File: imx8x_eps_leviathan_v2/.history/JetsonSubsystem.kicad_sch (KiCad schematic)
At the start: 32 parts, among them CN1 DF11-16DP-2DSA(08), U13 TPS1HB08BQPWPRQ1, U14 LT8612EUDE#PBF, U15 INA260AIPWR

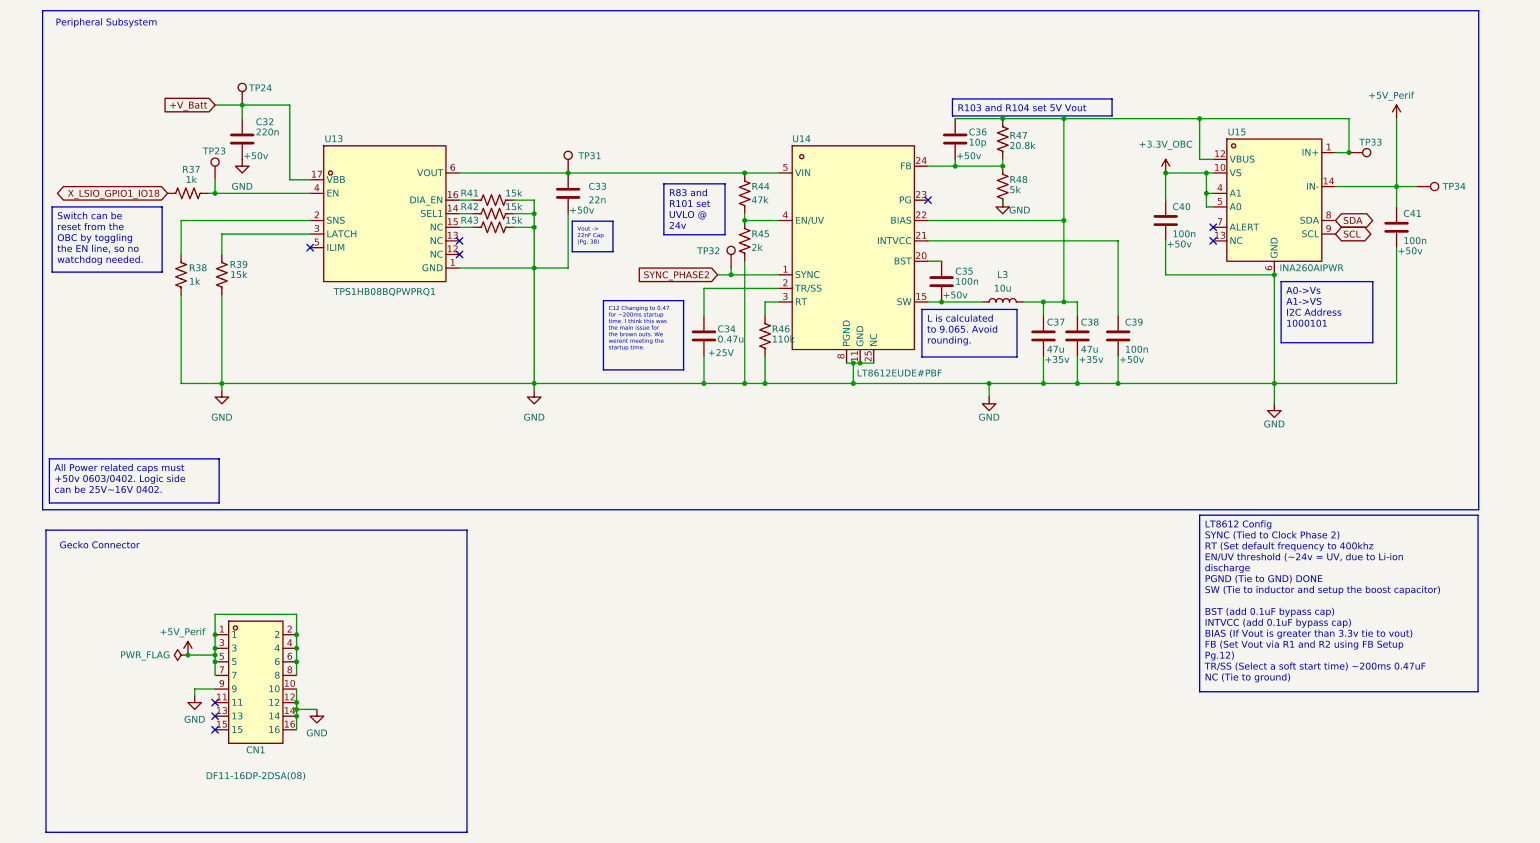
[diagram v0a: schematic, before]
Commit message: added R_Prot for CHA_GND
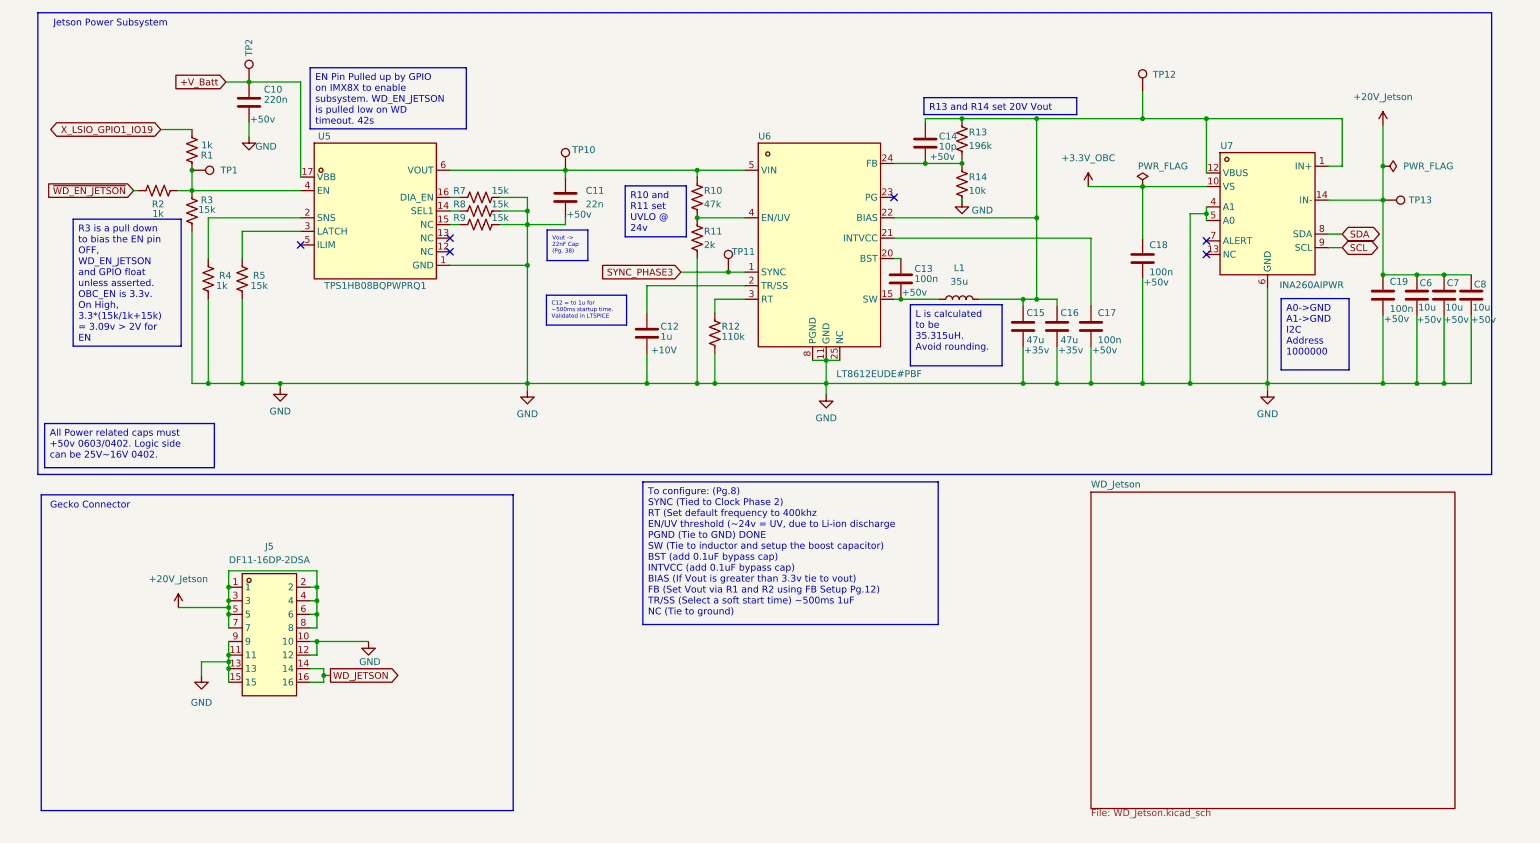
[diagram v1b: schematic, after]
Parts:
- removed C32: 220n, EPS:C0402, symbol Device:C
- removed C33: 22n, EPS:C0402, symbol Device:C
- removed C34: 0.47u, EPS:C0402, symbol Device:C
- removed C35, C39, C40, C41: 100n, EPS:C0402, symbol Device:C
- removed C36: 10p, EPS:C0402, symbol Device:C
- removed C37, C38: 47u, EPS:CAP-SMD_L7.3-W4.3-FD, symbol Device:C
- removed CN1: DF11-16DP-2DSA(08), EPS:CONN-TH_DF11-16DP-2DSA-08, symbol EPS:DF11-16DP-2DSA(08)
- removed L3: 10u, EPS:IND-SMD_L8.0-W8.0, symbol Device:L
- removed R37, R38: 1k, EPS:R0402, symbol Device:R_US
- removed R39, R41, R42, R43: 15k, EPS:R0402, symbol Device:R_US
- removed R44: 47k, EPS:R0402, symbol Device:R_US
- removed R45: 2k, EPS:R0402, symbol Device:R_US
- removed R46: 110k, EPS:R0402, symbol Device:R_US
- removed R47: 20.8k, EPS:R0402, symbol Device:R_US
- removed R48: 5k, EPS:R0402, symbol Device:R_US
- removed TP23, TP24, TP31, TP32, TP33, TP34: TestPoint, TestPoint:TestPoint_Pad_D1.0mm, symbol EPS:TestPoint
- removed U13: TPS1HB08BQPWPRQ1, EPS:HTSSOP-16_L5.0-W4.4-P0.65-LS6.4-TL-EP2.9, symbol EPS:TPS1HB08BQPWPRQ1
- removed U14: LT8612EUDE#PBF, EPS:QFN-28_L6.0-W3.0-P0.50-BL-EP, symbol EPS:LT8612EUDE#PBF
- removed U15: INA260AIPWR, EPS:TSSOP-16_L5.0-W4.4-P0.65-LS6.4-BL-1, symbol EPS:INA260AIPWR
- added C10: 220n, EPS:C0402, symbol Device:C
- added C11: 22n, EPS:C0402, symbol Device:C
- added C12: 1u, EPS:C0402, symbol Device:C
- added C13, C17, C18, C19: 100n, EPS:C0402, symbol Device:C
- added C14: 10p, EPS:C0402, symbol Device:C
- added C15, C16: 47u, EPS:CAP-SMD_L7.3-W4.3-FD, symbol Device:C
- added C6, C7, C8: 10u, Capacitor_SMD:C_1210_3225Metric, symbol Device:C
- added J5: DF11-16DP-2DSA, EPS:CONN-TH_DF11-16DP-2DSA-08, symbol EPS:DF11-16DP-2DSA(08)
- added L1: 35u, EPS:IND-SMD_L10.7-W10.0_ETQP5MXXXX, symbol Device:L
- added R1, R2, R4: 1k, EPS:R0402, symbol Device:R_US
- added R10: 47k, EPS:R0402, symbol Device:R_US
- added R11: 2k, EPS:R0402, symbol Device:R_US
- added R12: 110k, EPS:R0402, symbol Device:R_US
- added R13: 196k, EPS:R0402, symbol Device:R_US
- added R14: 10k, EPS:R0402, symbol Device:R_US
- added R3, R5, R7, R8, R9: 15k, EPS:R0402, symbol Device:R_US
- added TP1, TP10, TP11, TP12, TP13, TP2: TestPoint, TestPoint:TestPoint_Pad_D1.0mm, symbol EPS:TestPoint
- added U5: TPS1HB08BQPWPRQ1, EPS:HTSSOP-16_L5.0-W4.4-P0.65-LS6.4-TL-EP2.9, symbol EPS:TPS1HB08BQPWPRQ1
- added U6: LT8612EUDE#PBF, EPS:QFN-28_L6.0-W3.0-P0.50-BL-EP, symbol EPS:LT8612EUDE#PBF
- added U7: INA260AIPWR, EPS:TSSOP-16_L5.0-W4.4-P0.65-LS6.4-BL-1, symbol EPS:INA260AIPWR
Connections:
- net +3.3V_OBC: now also C18.1, U7.10 (VS)
- net +V_Batt: now also C10.1, TP2.1, U5.17 (VBB)
- net GND: now also C10.2, C11.2, C12.2, C15.2, C16.2, C17.2, C18.2, C19.2, C6.2, C7.2, C8.2, J5.10, J5.11, J5.12, J5.13, J5.15, J5.9, R11.2, R12.2, R14.2, R3.2, R4.1, R5.2, R7.2, R8.2, R9.2, U5.1 (GND), U6.11 (GND), U6.25 (NC), U6.8 (PGND), U7.4 (A1), U7.5 (A0), U7.6 (GND)
- net SCL: now also U7.9 (SCL)
- net SDA: now also U7.8 (SDA)
- new net: R8.1, U5.14 (SEL1)
- new net: C14.1, C15.1, C16.1, L1.2, R13.1, TP12.1, U6.22 (BIAS), U7.1 (IN+), U7.12 (VBUS)
- new net: R1.2, R2.1, R3.1, TP1.1, U5.4 (EN)
- new net: C11.1, R10.1, TP10.1, U5.6 (VOUT), U6.5 (VIN)
- new net: R10.2, R11.1, U6.4 (EN/UV)
- new net: C13.2, L1.1, U6.15 (SW)
- new net: C12.1, U6.2 (TR/SS)
- new net: C13.1, U6.20 (BST)
- new net: C17.1, U6.21 (INTVCC)
- new net: C14.2, R13.2, R14.1, U6.24 (FB)
- new net: R12.1, U6.3 (RT)
- new net: R9.1, U5.15 (NC)
- new net: R7.1, U5.16 (DIA_EN)
- new net: R4.2, U5.2 (SNS)
- new net: R5.1, U5.3 (LATCH)
- new net +20V_Jetson: C19.1, C6.1, C7.1, C8.1, J5.1, J5.2, J5.3, J5.4, J5.5, J5.6, J5.7, J5.8, TP13.1, U7.14 (IN-)
- new net SYNC_PHASE3: TP11.1, U6.1 (SYNC)
- new net WD_JETSON: J5.14, J5.16
- new net X_LSIO_GPIO1_IO19: R1.1
- new net ~{WD_EN_JETSON}: R2.2
- no-connect marks 9 -> 6
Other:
- added sheet WD_Jetson (WD_Jetson.kicad_sch)
- note added: "Jetson Power Subsystem"
- note removed: "Peripheral Subsystem"

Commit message: Goodies
Updated USB to USB C. Added Diodes for USB. Improved Layout. Ready for some routing.
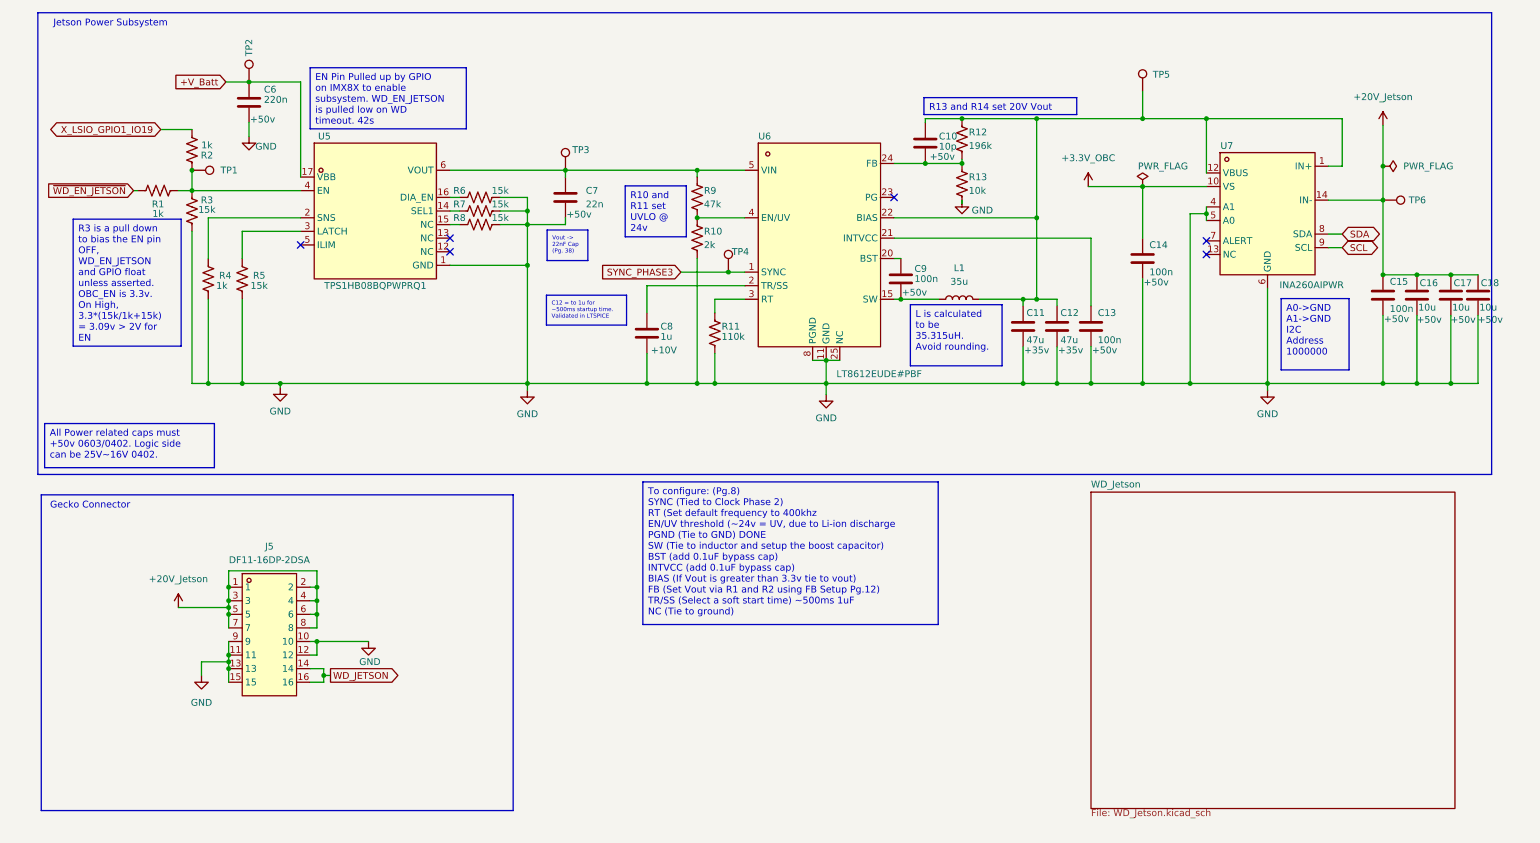
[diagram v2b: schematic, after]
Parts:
- removed C7, C8: 10u, Capacitor_SMD:C_1210_3225Metric, symbol Device:C
- added C17, C18: 10u, Capacitor_SMD:C_1210_3225Metric, symbol Device:C
- renumbered C14 to C10, C15 to C11, C16 to C12, C17 to C13, C18 to C14, C19 to C15, C6 to C16, C10 to C6, C11 to C7, C12 to C8, C13 to C9, R2 to R1, R11 to R10, R12 to R11, R13 to R12, R14 to R13, R1 to R2, R7 to R6, R8 to R7, R9 to R8, R10 to R9, TP10 to TP3, TP11 to TP4, TP12 to TP5, TP13 to TP6
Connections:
- net +20V_Jetson: now also C17.1, C18.1
- net GND: now also C17.2, C18.2
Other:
- title: Leviathan V1 -> Leviathan V2

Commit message: Updated Gerbers + BOM
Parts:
- renumbered J5 to CN3
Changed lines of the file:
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@@
 		(dnp no)
 		(fields_autoplaced yes)
-		(property "Reference" "J5"
+		(property "Reference" "CN3"
 			(at 57.15 114.3 0)
 			(show_name no)
@@
 			(project "imx8x_eps_leviathan_v2"
 				(path "/bd3af9f3-19df-4a2f-8b54-98c48cea082e/ec0c3356-3ab2-4b92-97c2-73704290dee9/638cb001-1cfc-4072-ab85-9425255a7df8"
-					(reference "J5")
+					(reference "CN3")
 					(unit 1)
 				)
